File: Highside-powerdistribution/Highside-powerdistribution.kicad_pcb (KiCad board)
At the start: 2 copper layers, 100 x 100 mm, 52 parts, among them J1 Conn_01x02_Male, J10 Screw_Terminal_01x02, J11 Screw_Terminal_01x02, J12 Screw_Terminal_01x02, J13 Screw_Terminal_01x02, J14 Conn_01x02, J15 Screw_Terminal_01x06, J2 Conn_01x02_Male, J3 Conn_01x02_Male, J4 Conn_01x02_Male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

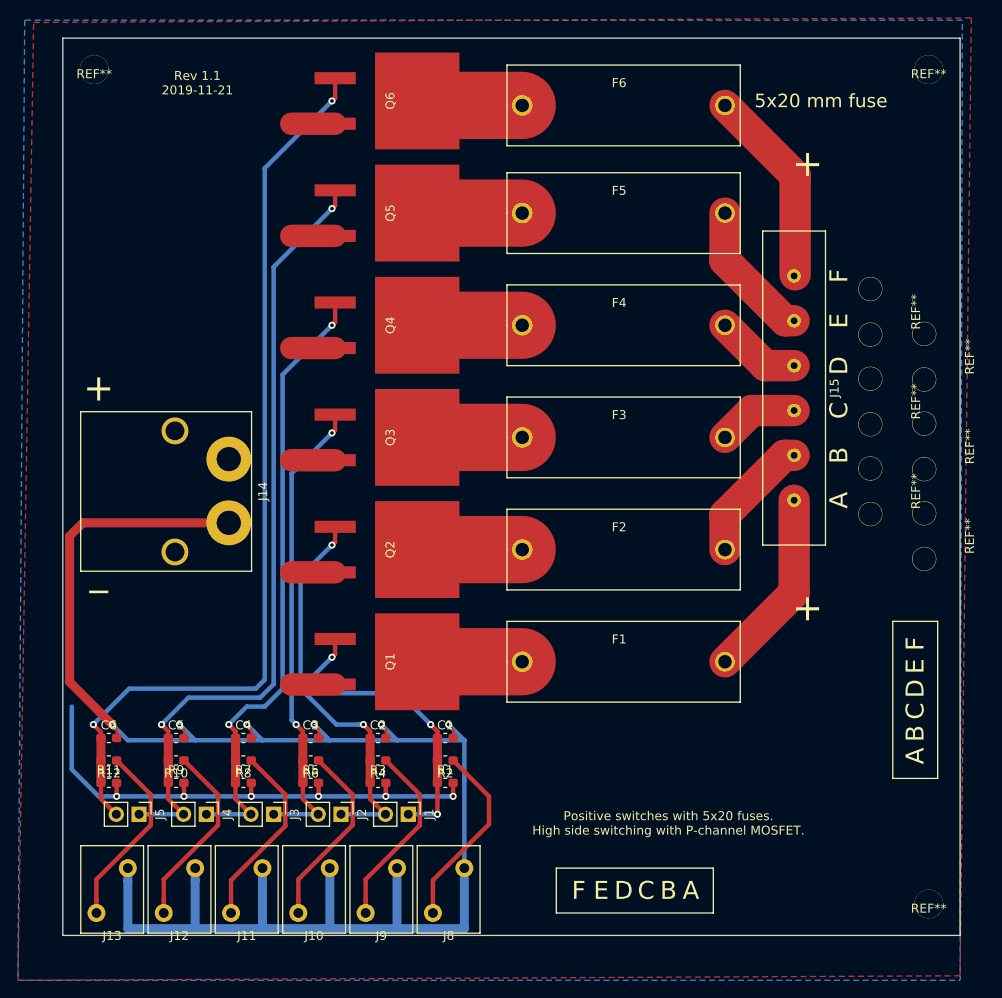
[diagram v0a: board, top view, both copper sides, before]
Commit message: Changed fuses and added more 3D files.
Changed to ATO fuses
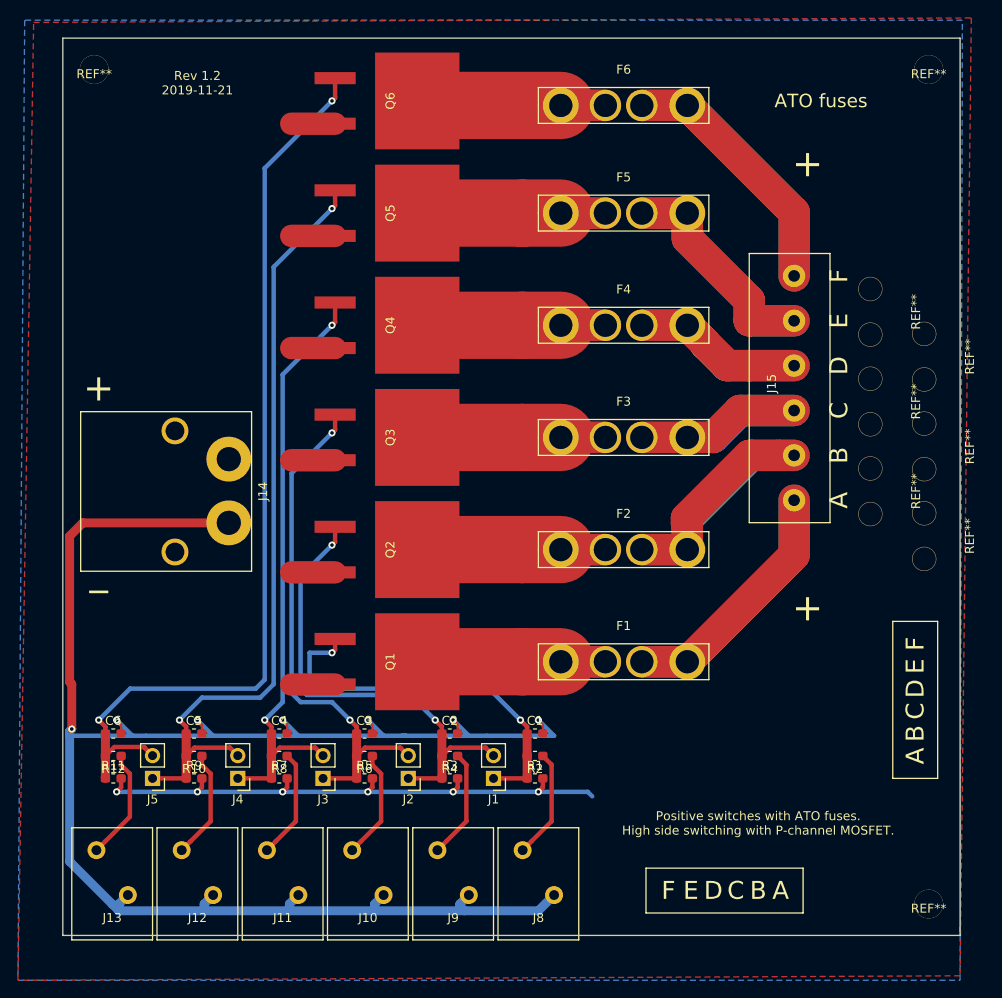
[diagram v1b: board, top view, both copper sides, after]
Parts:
- F1, F2, F3, F4, F5, F6: footprint Highside-powerdistribution:PTF-15 -> Highside-powerdistribution:ATO_Fuseholder_3522-2
- J10, J11, J12, J13, J8, J9: footprint Highside-powerdistribution:PTSA 1,5 2-3,5-Z -> Highside-powerdistribution:PTSA1,5-2-3,5-Z
- J15: footprint Highside-powerdistribution:ETB11060B000Z -> Highside-powerdistribution:20.101M-6
- moved J1 10.3 mm to (98.0, 132.5), turned to 180 degrees
- moved J8 10.2 mm to (103.0, 145.5)
- moved C1 10.0 mm to (102.6, 127.5)
- moved R1 10.0 mm to (102.6, 132.5)
- moved R2 10.0 mm to (102.6, 130.0)
- moved J2 8.50 mm to (88.5, 132.5), turned to 180 degrees
- moved J9 8.25 mm to (93.5, 145.5)
- moved C2 8.02 mm to (93.1, 127.5)
- moved R3 8.02 mm to (93.1, 132.5)
- moved R4 8.02 mm to (93.1, 130.0)
- moved J3 6.80 mm to (79.0, 132.5), turned to 180 degrees
- moved J10 6.32 mm to (84.0, 145.5)
- moved C3 6.02 mm to (83.6, 127.5)
- moved R5 6.02 mm to (83.6, 132.5)
- moved R6 6.02 mm to (83.6, 130.0)
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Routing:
- net Net-(F6-Pad1): track 22.1 -> 58.0 mm
- net Net-(F1-Pad1): track 21.2 -> 56.0 mm
- net Net-(F5-Pad1): track 15.8 -> 49.9 mm
- net Net-(F2-Pad1): track 14.3 -> 46.8 mm
- net Net-(F4-Pad1): track 9.56 -> 37.7 mm
- net Net-(F3-Pad1): track 8.94 -> 36.4 mm
- net SSR-E: track 11.7 -> 25.9 mm
- net SSR-D: track 11.7 -> 25.9 mm
- net SSR-C: track 11.7 -> 25.9 mm
- net SSR-B: track 11.7 -> 25.9 mm
- net SSR-A: track 11.7 -> 25.9 mm
- net SSR-F: track 11.9 -> 26.1 mm
- net Net-(J8-Pad1): track 21.2 -> 12.2 mm
- net Net-(C2-Pad1): track 44.3 -> 53.2 mm
- net Net-(J9-Pad1): track 21.1 -> 12.2 mm
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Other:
- board text added: "ATO fuses"
- board text added: "Positive switches with ATO fuses. High side switching with P-channel MOSFET."
- board text added: "Rev 1.2 2019-11-21"
- board text removed: "5x20 mm fuse"
- board text removed: "Positive switches with 5x20 fuses. High side switching with P-channel MOSFET."
- board text removed: "Rev 1.1 2019-11-21"

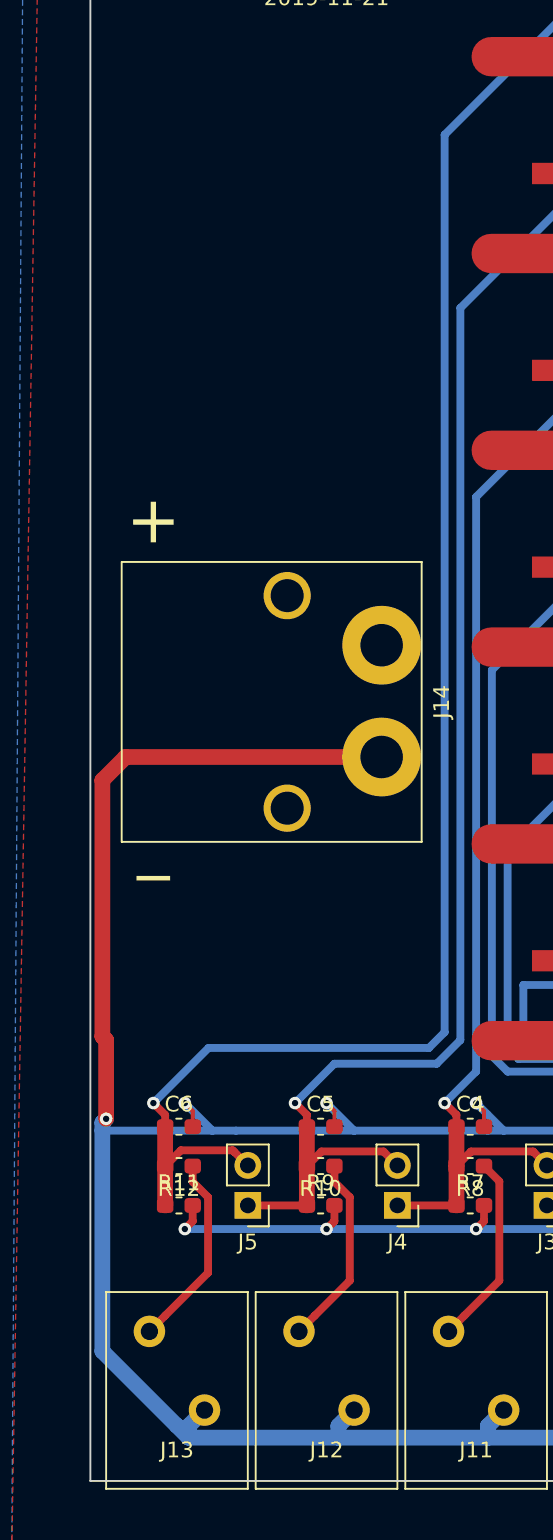
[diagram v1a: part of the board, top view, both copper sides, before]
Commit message: Changed to terminal block on input
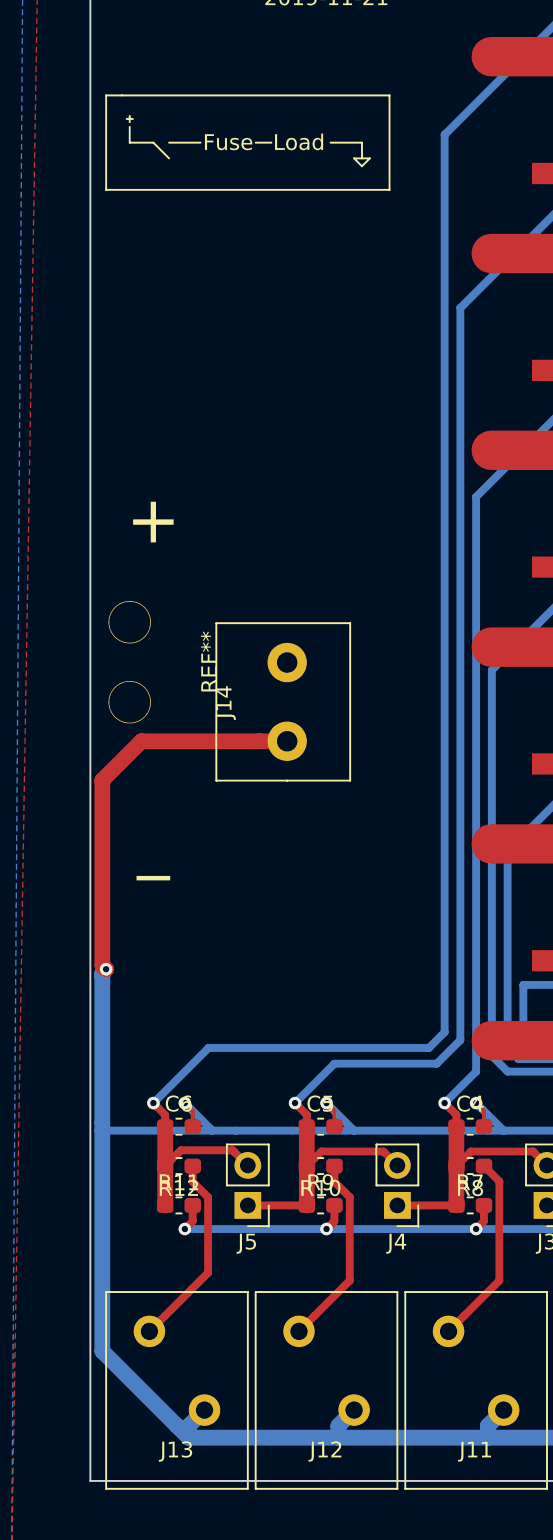
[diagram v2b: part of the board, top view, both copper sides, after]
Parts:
- added REF**: WireDistresser, Highside-powerdistribution:WireDistresser, F.Cu at (52.5, 98.0)
- J14: footprint Highside-powerdistribution:XT60PW-F -> Highside-powerdistribution:Phoenix_TB_2-1935776
- moved J14 6.00 mm to (62.5, 100.5), turned to 270 degrees
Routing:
- net GND: track 202.4 -> 196.8 mm
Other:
- board text added: "Fuse"
- board text added: "Load"

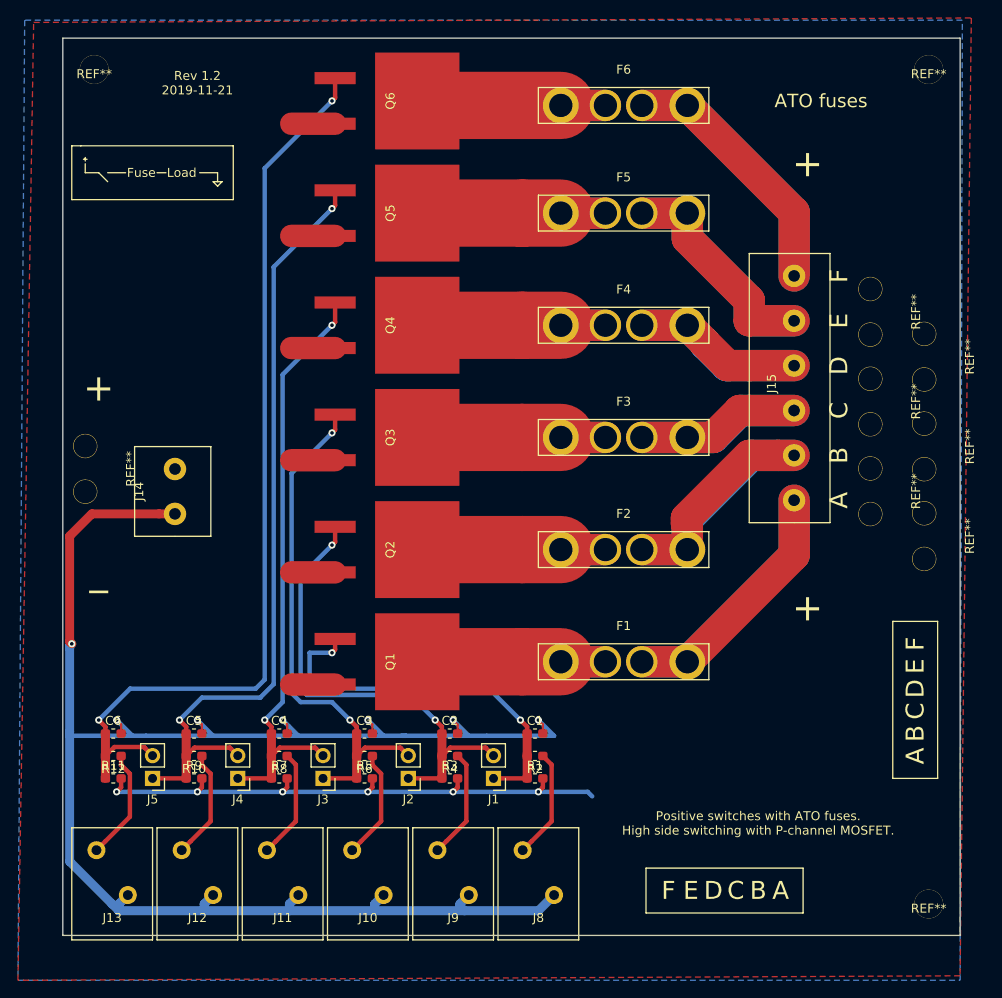
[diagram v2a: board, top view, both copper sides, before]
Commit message: Updated schematic with Powersplitter added
Big commit with added powersplitter and updated power distribution board.
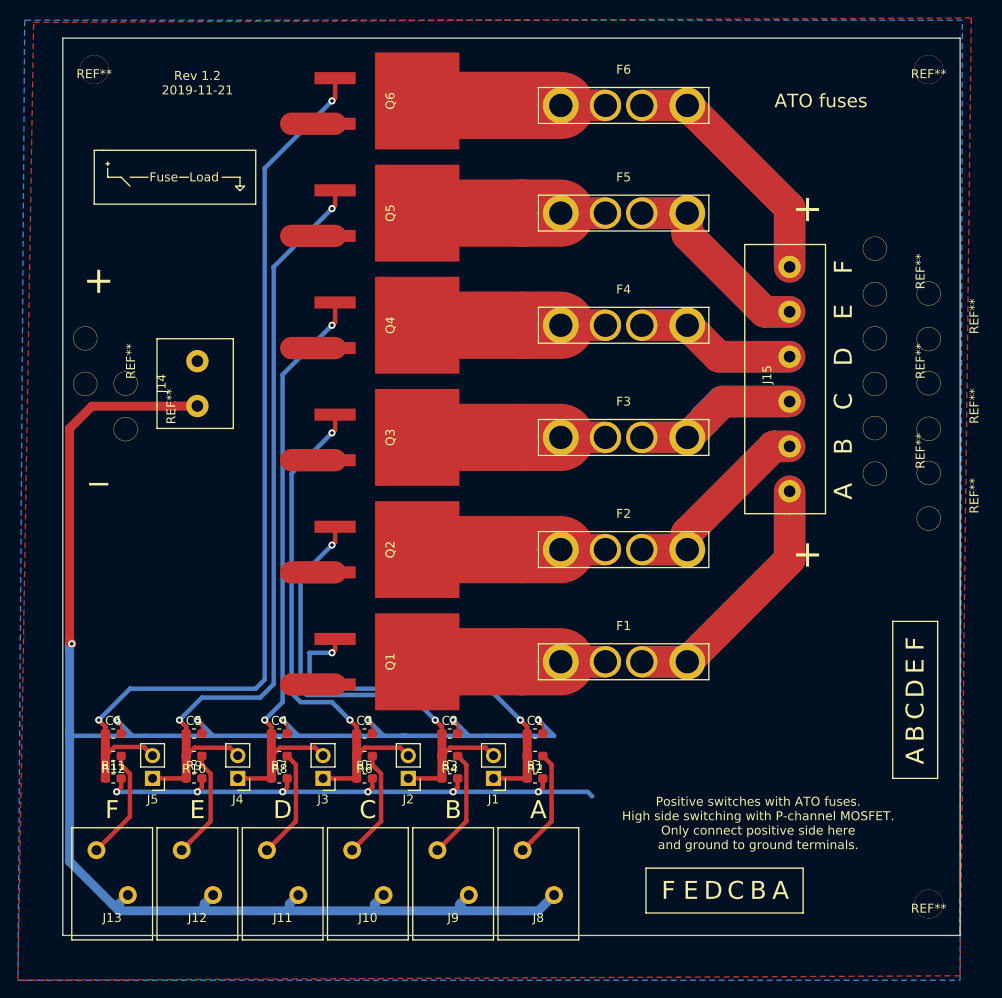
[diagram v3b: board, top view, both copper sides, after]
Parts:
- removed the REF** at (140.0, 80.5)
- removed the REF** at (146.0, 105.5)
- removed the REF** at (146.0, 95.5)
- removed the REF** at (140.0, 100.5)
- removed the REF** at (140.0, 90.5)
- removed the REF** at (146.0, 85.5)
- added REF**: WireDistresser, Highside-powerdistribution:WireDistresser, F.Cu at (57.0, 91.0)
- added REF**: WireDistresser, Highside-powerdistribution:WireDistresser, F.Cu at (146.5, 81.0)
- added REF**: WireDistresser, Highside-powerdistribution:WireDistresser, F.Cu at (140.5, 76.0)
- added REF**: WireDistresser, Highside-powerdistribution:WireDistresser, F.Cu at (146.5, 101.0)
- added REF**: WireDistresser, Highside-powerdistribution:WireDistresser, F.Cu at (146.5, 91.0)
- added REF**: WireDistresser, Highside-powerdistribution:WireDistresser, F.Cu at (140.5, 96.0)
- added REF**: WireDistresser, Highside-powerdistribution:WireDistresser, F.Cu at (140.5, 86.0)
- moved J14 12.3 mm to (65.0, 88.5)
- moved REF** 12.0 mm to (52.5, 86.0)
- moved J15 1.12 mm to (131.0, 88.0)
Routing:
- net GND: track 196.8 -> 211.3 mm
- net Net-(F5-Pad1): track 49.9 -> 44.9 mm
- net Net-(F6-Pad1): track 58.0 -> 55.6 mm
- net Net-(F2-Pad1): track 46.8 -> 44.8 mm
- net Net-(F4-Pad1): track 37.7 -> 35.8 mm
- net Net-(F1-Pad1): track 56.0 -> 57.6 mm
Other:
- board text added: "Positive switches with ATO fuses. High side switching with P-channel MOSFET. Only connect positive side here and ground to ground terminals."
- board text removed: "Positive switches with ATO fuses. High side switching with P-channel MOSFET."
